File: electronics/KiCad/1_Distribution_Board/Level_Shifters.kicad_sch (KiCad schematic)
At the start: 32 parts, among them J10 Generic 2.54mm, J11 Generic 2.54mm, J5 Generic 2.54mm, J6 Generic 2.54mm, J8 Generic 2.54mm, J9 Generic 2.54mm, Q2 AO3400A, Q3 AO3400A, Q4 AO3400A, Q5 AO3400A

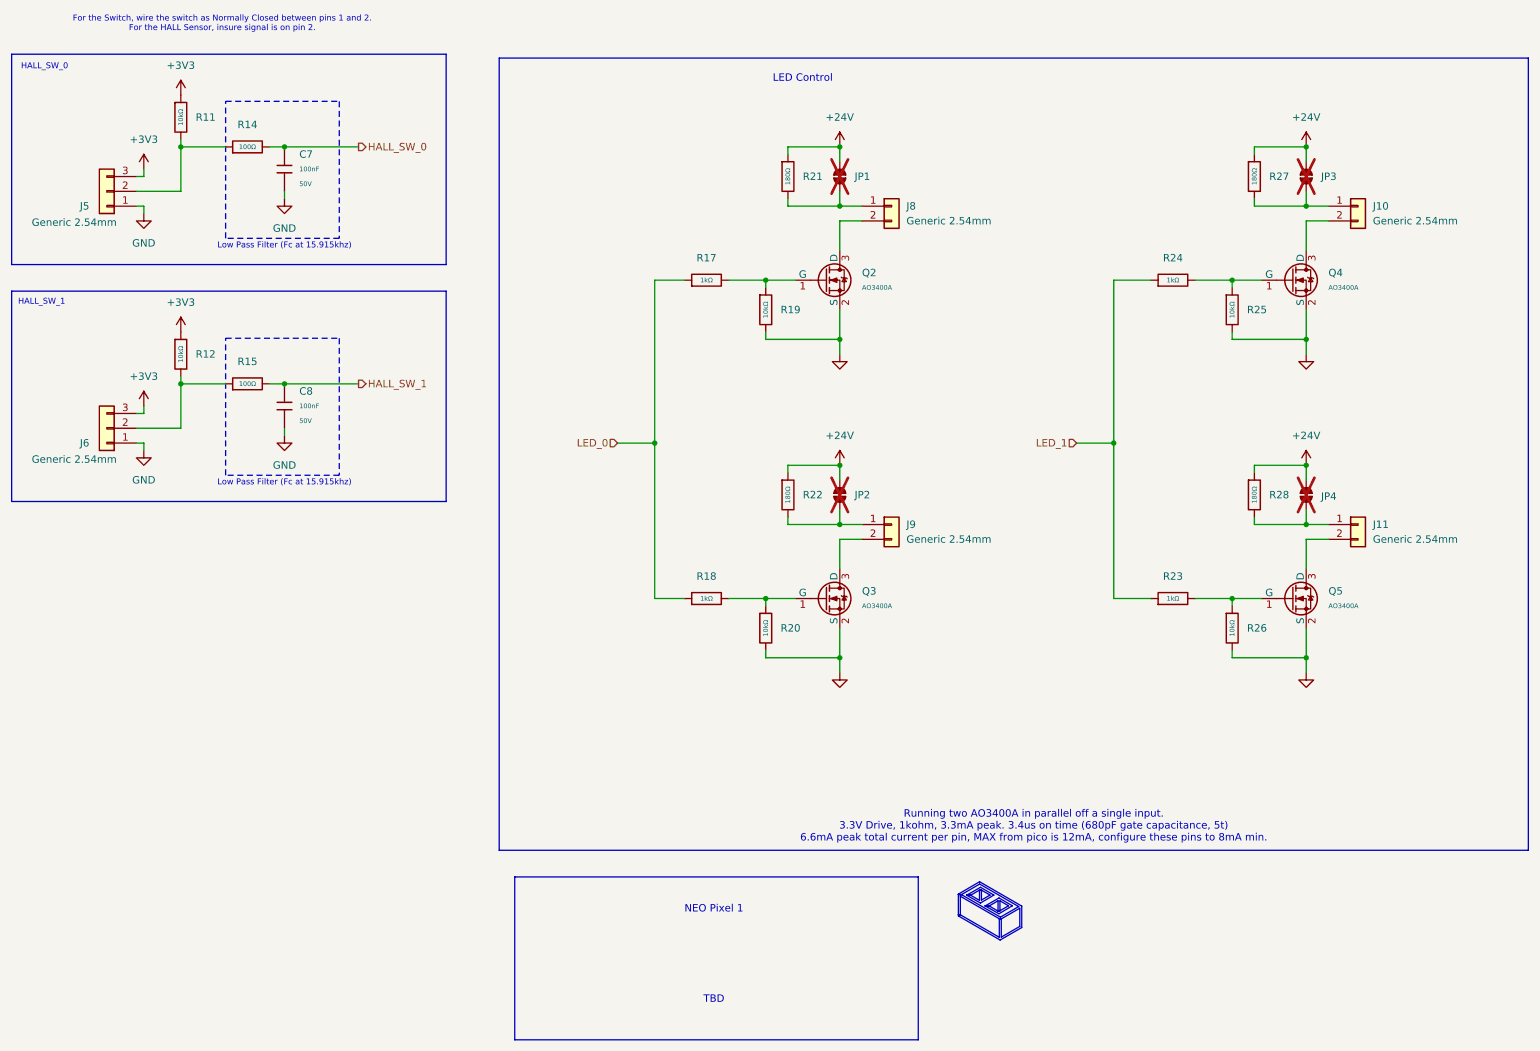
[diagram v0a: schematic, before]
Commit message: Distribution board v1.4.1: effreek's revision, REV label, JLC rotation offsets restored (#1169)
effreek's pull-up/pull-down cleanup and test serial-servo circuit (J11/J14/J15), REV 1.4.1 on the board, the 33 JLC rotation offsets restored, test points out of the position file, and the V1.4.1 Gerber zip. Supersedes #1042.

Co-authored-by: effreek <115494910+effreek@users.noreply.github.com>
Co-Authored-By: Claude Opus 5.5 <noreply@anthropic.com>
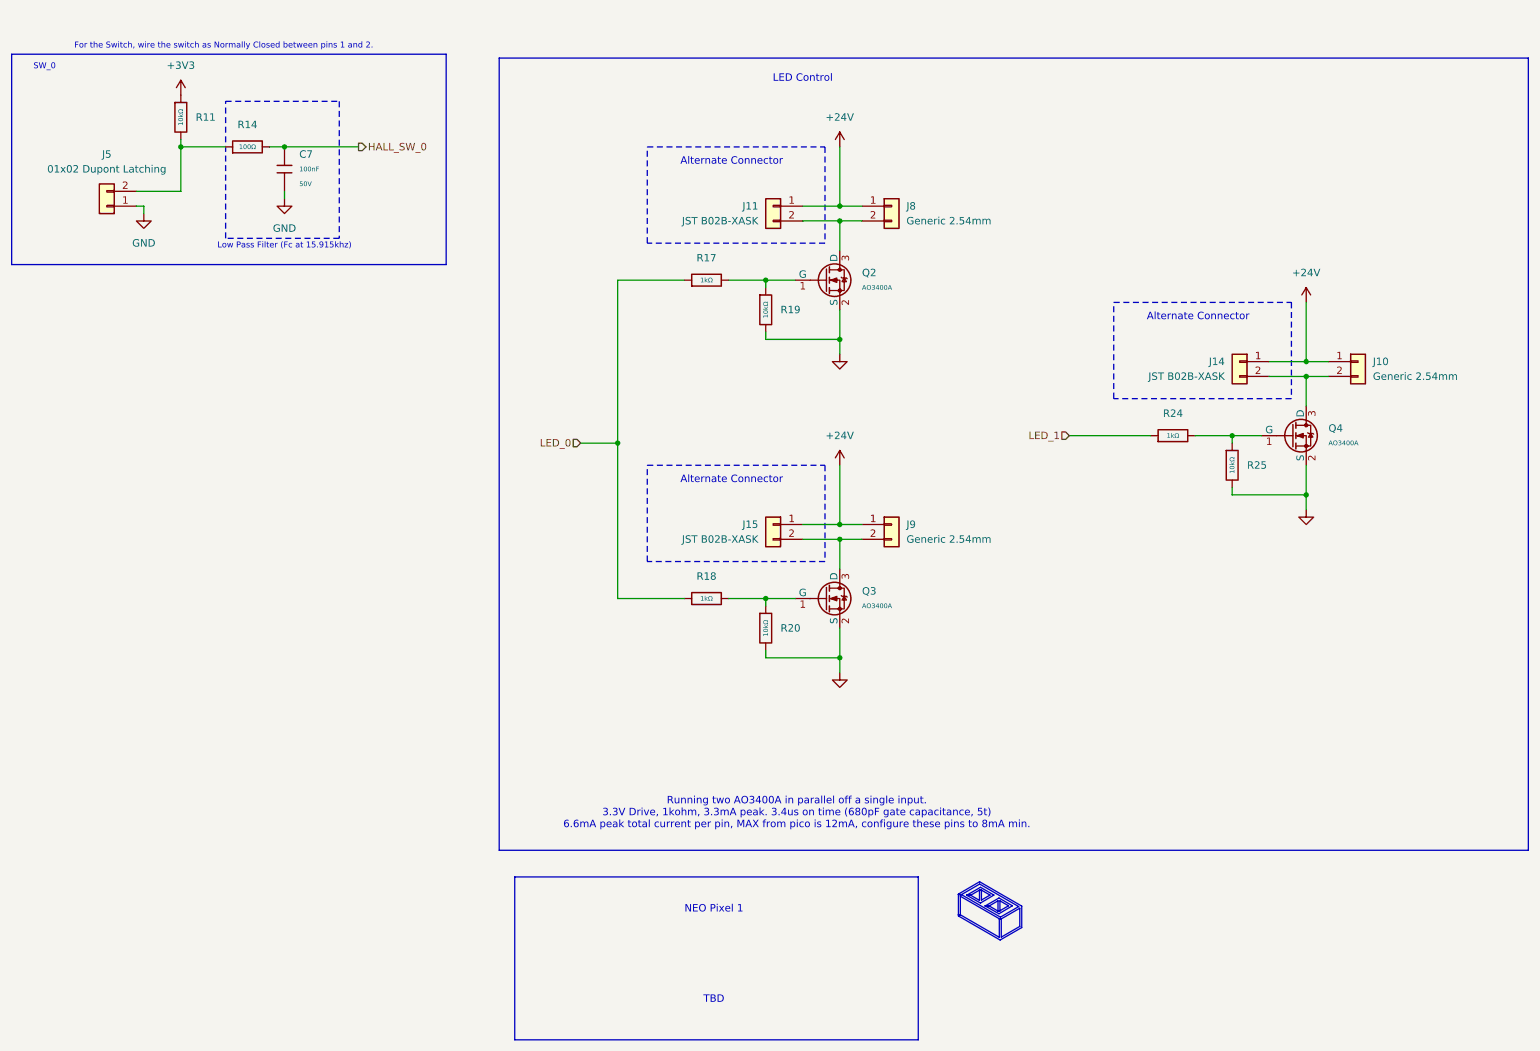
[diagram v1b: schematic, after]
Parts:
- removed C8: 100nF, PCM_JLCPCB:C_0603, symbol PCM_JLCPCB-Capacitors:0603,100nF
- removed J5, J6: Generic 2.54mm, Connector_PinHeader_2.54mm:PinHeader_1x03_P2.54mm_Vertical, symbol Connector_Generic:Conn_01x03
- removed JP1, JP2, JP3, JP4: ~, PCM_SparkFun-Jumper:Jumper_2_NO, symbol PCM_SparkFun-Jumper:SolderJumper_2_Open
- removed Q5: AO3400A, PCM_JLCPCB:Q_SOT-23, symbol PCM_JLCPCB-Transistors:NMOS,AO3400A
- removed R12, R26: 10kΩ, PCM_JLCPCB:R_0603, symbol PCM_JLCPCB-Resistors:0603,10kΩ
- removed R15: 100Ω, PCM_JLCPCB:R_0603, symbol PCM_JLCPCB-Resistors:0603,100Ω
- removed R21, R22, R27, R28: 180Ω, PCM_JLCPCB:R_1206, symbol PCM_JLCPCB-Resistors:1206,180Ω
- removed R23: 1kΩ, PCM_JLCPCB:R_0603, symbol PCM_JLCPCB-Resistors:0603,1kΩ
- added J14, J15: JST B02B-XASK, Connector_JST:JST_XA_B02B-XASK-1-A_1x02_P2.50mm_Vertical, symbol Connector_Generic:Conn_01x02
- added J5: 01x02 Dupont Latching, Connector_Molex:Molex_SL_171971-0002_1x02_P2.54mm_Vertical, symbol Connector_Generic:Conn_01x02
- J11: value Generic 2.54mm -> JST B02B-XASK; footprint Connector_PinHeader_2.54mm:PinHeader_1x02_P2.54mm_Vertical -> Connector_JST:JST_XA_B02B-XASK-1-A_1x02_P2.50mm_Vertical; LCSC C492401 -> C265077
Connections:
- net +24V: now also J10.1 (Pin_1), J11.1 (Pin_1), J8.1 (Pin_1), J9.1 (Pin_1), J14.1 (Pin_1), J15.1 (Pin_1)
- net GND: now also J5.1 (Pin_1)
- net at R11.2, R14.1: now also J5.2 (Pin_2)
- net at J8.2 (Pin_2), Q2.3 (D): now also J11.2 (Pin_2)
- net at J9.2 (Pin_2), Q3.3 (D): now also J15.2 (Pin_2)
- net at J10.2 (Pin_2), Q4.3 (D): now also J14.2 (Pin_2)
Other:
- note added: "Alternate Connector"
- note added: "For the Switch, wire the switch as Normally Closed between pins 1 and 2."
- note added: "SW_0"
- note removed: "For the Switch, wire the switch as Normally Closed between pins 1 and 2. For the HALL Sensor, insure signal is on pin 2."
- note removed: "HALL_SW_0"
- note removed: "HALL_SW_1"
- moved on the sheet: J10, Q4, R24, R25
